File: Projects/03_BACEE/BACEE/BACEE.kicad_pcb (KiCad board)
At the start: 2 copper layers, 44.7 x 28.4 mm, 17 parts, among them J1 Digital Pins, J2 Serial, J3 ICSP, J4 I2C, U1 DS1337_MLv1, U2 24LC1025, U3 24LC1025, U4 ATmega328P-AU, Y1 Crystal 32MHz, Y2 Crystal 16MHz

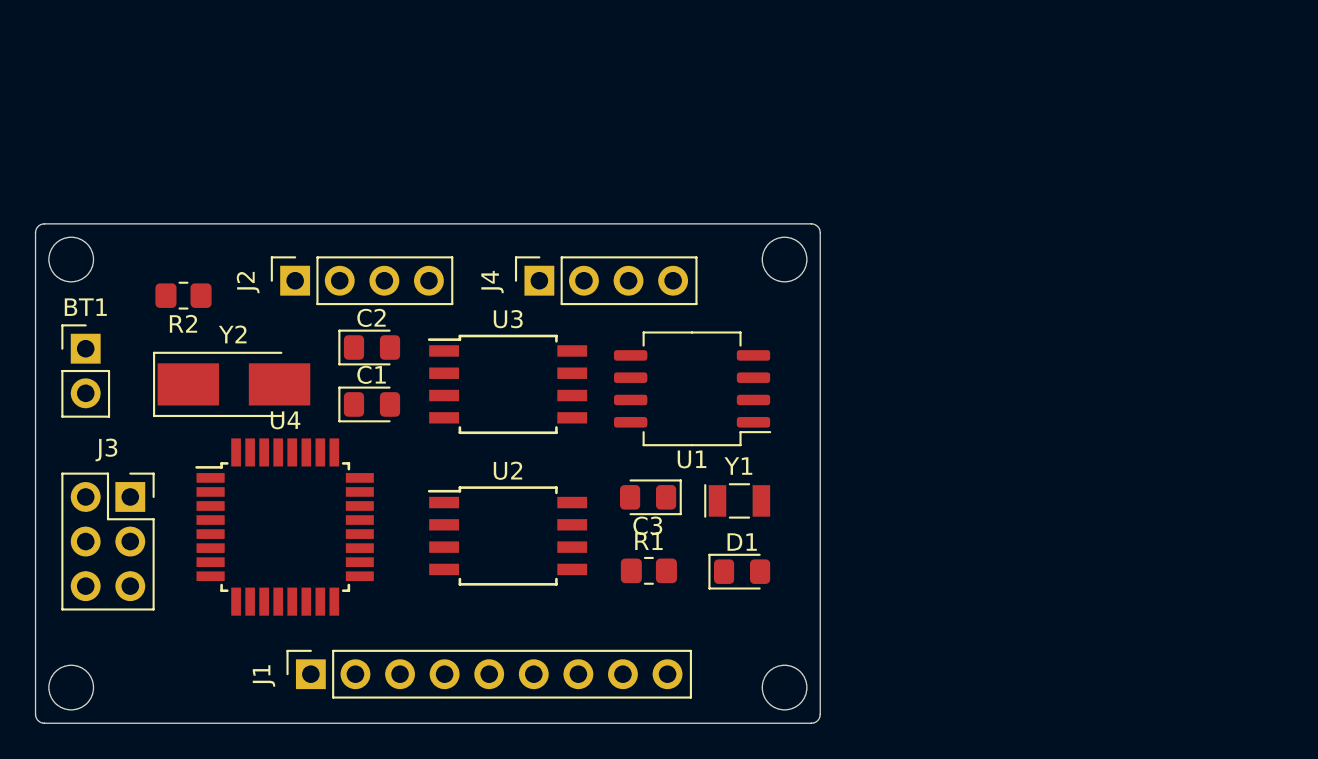
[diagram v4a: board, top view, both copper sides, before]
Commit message: Project 3: Rearrange board components closer and align headers for 4-layer board
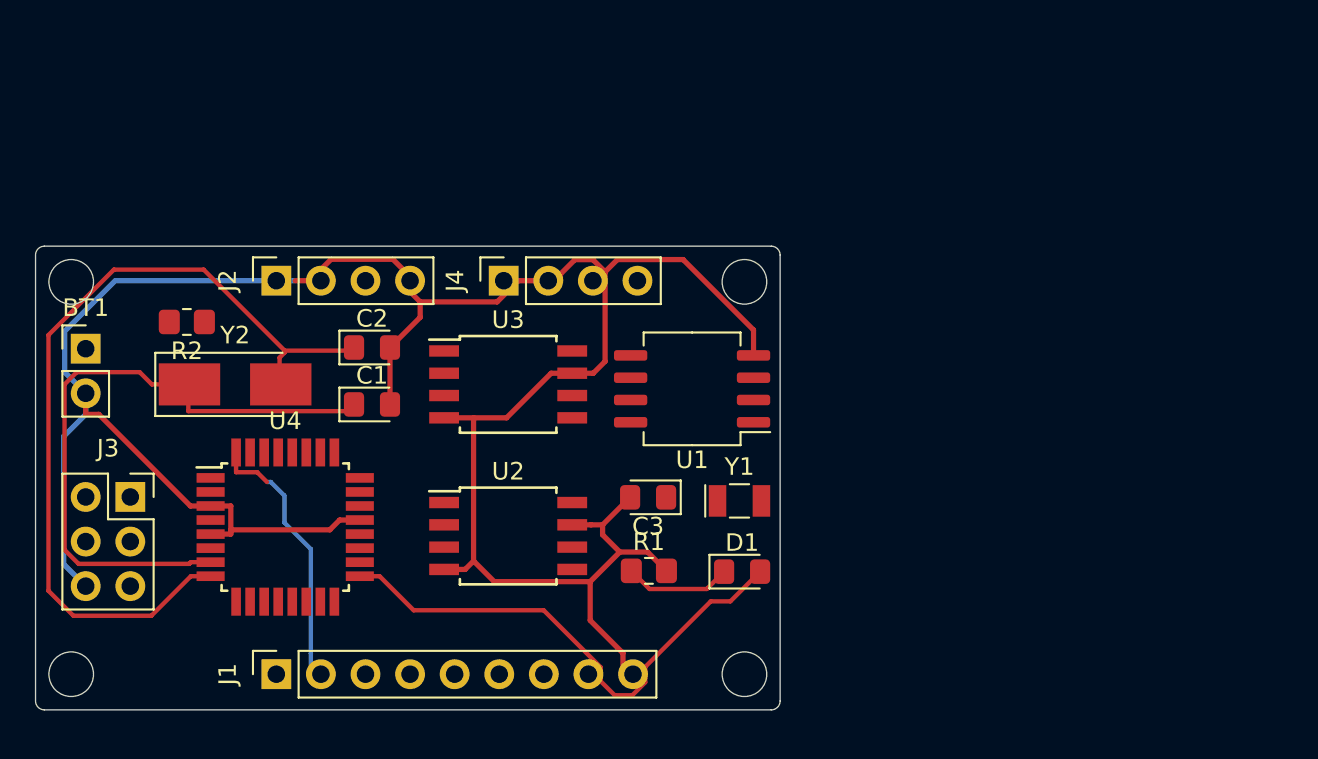
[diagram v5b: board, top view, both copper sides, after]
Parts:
- moved J4 2.03 mm to (229.4, 103.8)
- moved J1 1.97 mm to (216.4, 126.2)
- moved R2 1.51 mm to (211.3, 106.2)
- moved J2 1.07 mm to (216.4, 103.8)
- moved Y2 0.07 mm to (214.1, 109.7)
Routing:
- net GNDPWR: track 0.00 -> 142.4 mm
- net Net-(C2-Pad1): track 0.00 -> 48.3 mm
- net Net-(C1-Pad1): track 0.00 -> 36.9 mm
- net Net-(D1-Pad2): track 0.00 -> 29.5 mm
- net /D3: track 0.00 -> 12.1 mm
- net Net-(D1-Pad1): track 0.00 -> 6.12 mm
- net /D2: track 0.00 -> 3.11 mm
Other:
- board size 44.7 x 28.4 mm -> 42.4 x 26.4 mm
- copper layers 2 -> 4

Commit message: Project 3: Route 4-layer board again
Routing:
- net GNDPWR: track 142.4 -> 0.00 mm
- net Net-(C2-Pad1): track 48.3 -> 0.00 mm
- net Net-(C1-Pad1): track 36.9 -> 0.00 mm
- net Net-(D1-Pad2): track 29.5 -> 0.00 mm
- net /D3: track 12.1 -> 0.00 mm
- net Net-(D1-Pad1): track 6.12 -> 0.00 mm
- net /D2: track 3.11 -> 0.00 mm

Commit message: Project3: Set design rules for 2-layer board
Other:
- copper layers 4 -> 2
